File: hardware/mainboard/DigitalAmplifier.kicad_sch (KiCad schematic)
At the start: 53 parts, among them J10 FFC2B35-10-T, J12 Conn_01x02, J2 Conn_01x02, J3 Conn_01x02, J4 Conn_01x02, J5 USB4215-03-A_REVA, J6 Conn_01x02, J7 43045-0400, J9 Conn_01x02, U1 ORJ-3__FCR6842032R_

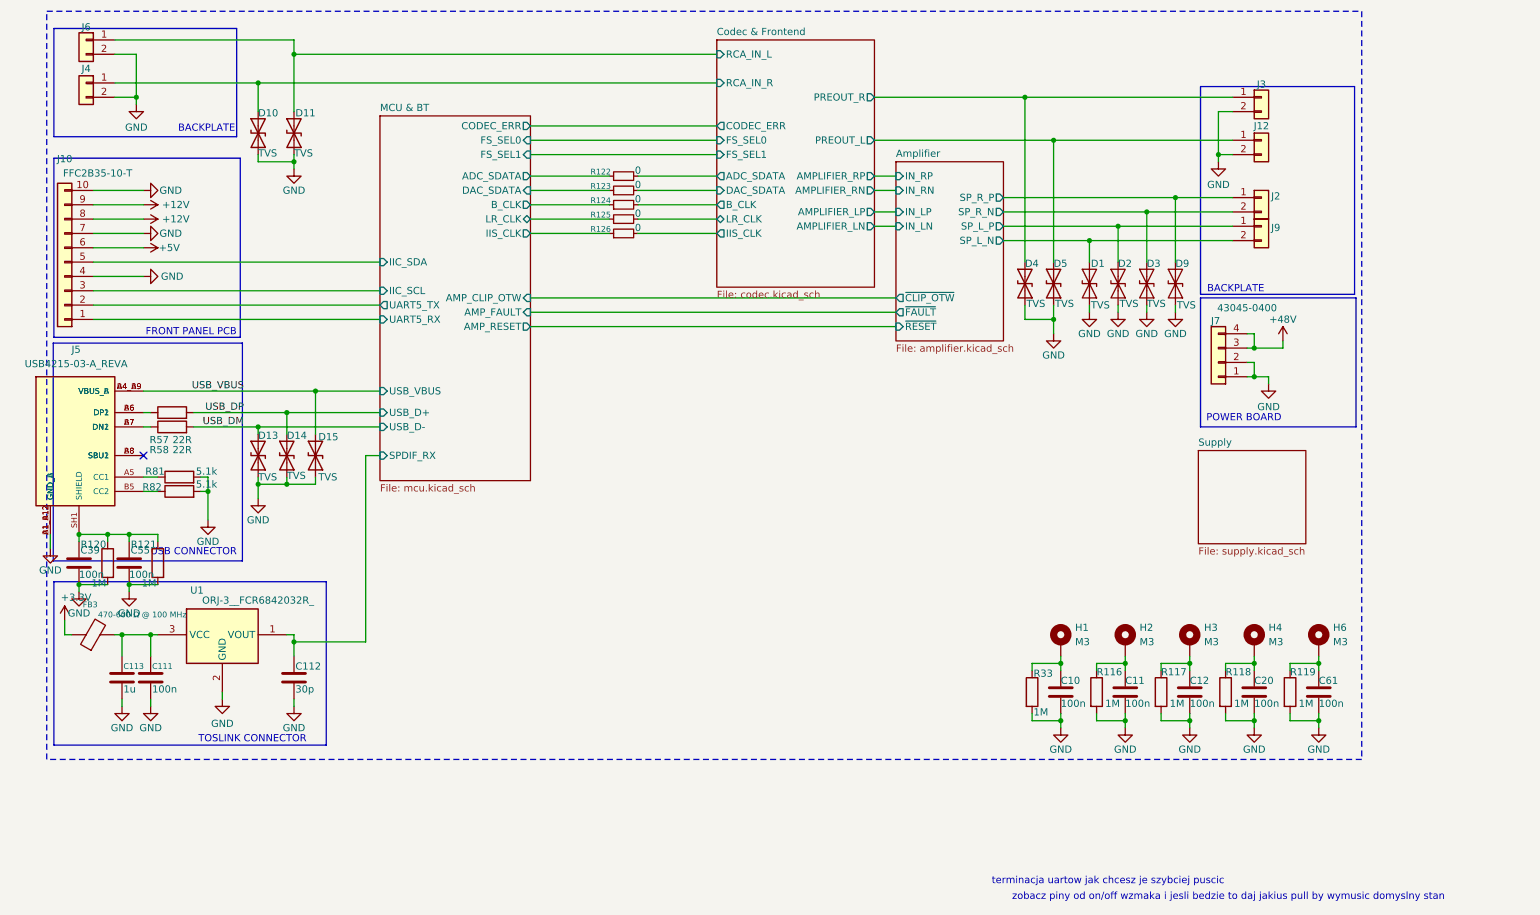
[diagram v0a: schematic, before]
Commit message: Add power supply and front panel PCBs
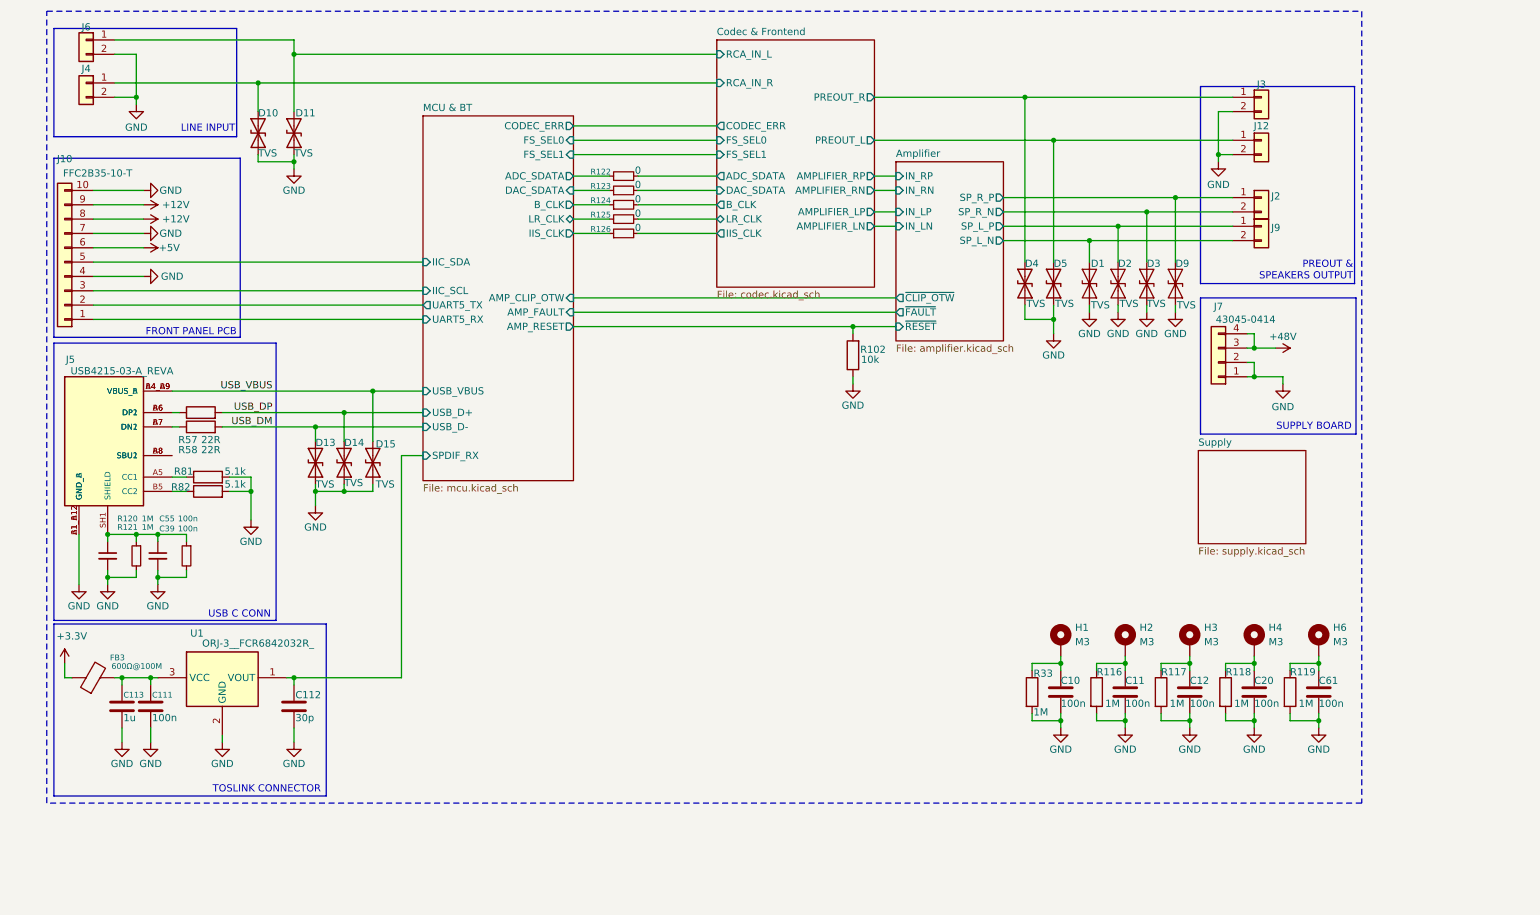
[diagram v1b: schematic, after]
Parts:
- added R102: 10k, Resistor_SMD:R_0603_1608Metric, symbol Device:R
- C39, C55: symbol Device:C -> Device:C_Small
- FB3: value 470-600 Ω @ 100 MHz -> 600Ω@100M
- J7: value 43045-0400 -> 43045-0414; footprint digital_amp:43045-04_00,01,02,10_ -> digital_amp:43045-04YY_121314
- R120, R121: symbol Device:R -> Device:R_Small
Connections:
- net Amplifier/~{RESET}: now also R102.2
- net GND: now also R102.1
- no-connect marks 1 -> 0
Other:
- note added: "LINE INPUT"
- note added: "PREOUT & SPEAKERS OUTPUT"
- note added: "SUPPLY BOARD"
- note added: "USB C CONN"
- note removed: "BACKPLATE"
- note removed: "POWER BOARD"
- note removed: "USB CONNECTOR"
- note removed: "terminacja uartow jak chcesz je szybciej puscic"
- note removed: "zobacz piny od on/off wzmaka i jesli bedzie to daj jakius pull by wymusic domyslny stan"
- moved on the sheet: C111, C112, C113, C39, C55, D13, D14, D15, FB3, J5, R120, R121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

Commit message: Prepare PCB for production
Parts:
- removed J12, J3, J4, J6: Conn_01x02, digital_amp:RF219AT0050G, symbol Connector_Generic:Conn_01x02
- added J3, J4: 3P HEADER, Connector_JST:JST_PH_B3B-PH-K_1x03_P2.00mm_Vertical, symbol Connector_Generic:Conn_01x03
- C10, C11, C111, C12, C20, C39, C55, C61: Manufacturer_Part_Number (none) -> 0603B104K500CT
- C112: Manufacturer_Part_Number (none) -> C0603C300J5GACTU
- C113: Manufacturer_Part_Number (none) -> CL10A105KB8NNNC
- H1, H2, H3, H4, H6: Manufacturer_Part_Number (none) -> 9774040360R
- J10: Manufacturer_Part_Number (none) -> FFC2B3510T
- J2, J9: Manufacturer_Part_Number (none) -> 43650-0215
- J5: Manufacturer_Part_Number (none) -> GCT_USB4215-03-A_REVA
- J7: Manufacturer_Part_Number (none) -> 43045-04YY_121314
- R102: Manufacturer_Part_Number (none) -> RC0603JR-0710KL
- R116, R117, R118, R119, R120, R121, R33: Manufacturer_Part_Number (none) -> RC0603JR-071ML
- R122, R123, R124, R125, R126: Manufacturer_Part_Number (none) -> RC0402JR-070RL
- R57, R58: Manufacturer_Part_Number (none) -> WR06X220 JTL
- R81, R82: Manufacturer_Part_Number (none) -> WR06X5101FTL
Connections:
- net Codec & Frontend/PREOUT_L: now also J3.3 (Pin_3)
- net Codec & Frontend/PREOUT_R: now also J3.1 (Pin_1)
- net Codec & Frontend/RCA_IN_L: now also J4.1 (Pin_1)
- net Codec & Frontend/RCA_IN_R: now also J4.3 (Pin_3)
- net GND: now also J3.2 (Pin_2), J4.2 (Pin_2)
